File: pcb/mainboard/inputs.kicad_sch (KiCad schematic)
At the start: 95 parts

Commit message: Continued initial work on main board
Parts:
- added C122: 4.7 uF, symbol device:C
- added C123: 0.47 uF, symbol device:C
- added U30: SIT9121AI-2BF-XXS200.000000G, symbol osc-azonenberg:OSC_LVDS_NOPAD
- R101, R102: renamed from R?; footprint azonenberg_pcb:EIA_0402_RES_NOSILK -> (none)
- U8: renamed from U?; footprint azonenberg_pcb:BGA_484_22x22_FULLARRAY_1MM -> (none)
- gave numbers to parts that had none: 92
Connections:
- net 3V3: now also C122.1, C123.1, U30.1 (EN), U30.6 (VDD); no longer C73.1, C74.1, U21.7 (VDD), U22.7 (VDD)
- net DAC0_VREF: now also U21.1 (REF)
- net GND: now also C122.2, C123.2, U30.3 (GND)
- net VREF_SERDESIN: now reaches U22.11 (OUT7)
- net CLK_200_P: now reaches U8.R3 (IO_L12P_T1_MRCC_34)
- net CLK_200_P: now also U30.4 (OUT_P)
- net CLK_200_N: now reaches U8.T3 (IO_L12N_T1_MRCC_34)
- net CLK_200_N: now also U30.5 (OUT_N)
- new net 5V0: C73.1, C74.1, U21.7 (VDD), U22.7 (VDD)
- no-connect marks 4 -> 25
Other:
- note removed: "TODO: LVDS clock oscillator as main FPGA clock source"

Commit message: Calculated power monitor voltage divider
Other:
- company: (none) -> Antikernel Labs
- title: (none) -> Trigger Crossbar
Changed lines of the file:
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@@
 (kicad_sch (version 20211123) (generator eeschema)
   (paper "A2")
+  (title_block
+    (title "Trigger Crossbar")
+    (date "2023-12-17")
+    (rev "0.1")
+    (company "Antikernel Labs")
+    (comment 1 "Andrew D. Zonenberg")
+  )
   (junction (at 31.75 264.16) (diameter 0) (color 0 0 0 0)
   )

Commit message: Began assigning footprints
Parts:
- C122: footprint (none) -> azonenberg_pcb:EIA_0603_CAP_NOSILK
- C123, C59, C60, C61, C62, C63, C64, C65, C66, C67, C68, C69, C70, C71, C72, C73, C74, C75, C76: footprint (none) -> azonenberg_pcb:EIA_0402_CAP_NOSILK
- D10, D11, D12, D13, D14, D3, D4, D5, D6, D7, D8, D9: footprint (none) -> azonenberg_pcb:SOD882
- R100, R101, R102, R53, R54, R55, R56, R57, R58, R59, R60, R61, R62, R63, R64, R65, R66, R67, R68, R69, R70, R71, R72, R73, R74, R75, R76, R77, R78, R79, R80, R81, R82, R83, R84, R85, R86, R87, R88, R89, R90, R91, R92, R93, R94, R95, R96, R97, R98, R99: footprint (none) -> azonenberg_pcb:EIA_0402_RES_NOSILK
- U10, U11, U12, U13, U14, U15, U16, U17, U18, U19, U20, U9: footprint (none) -> azonenberg_pcb:DFN_8_0.5MM_2x2MM
- U21, U22: value DACx0508_WQFN -> DAC60508; footprint (none) -> azonenberg_pcb:QFN_16_0.5MM_3x3MM
- U30: footprint (none) -> azonenberg_pcb:OSCILLATOR_LVDS_3.2x2.5
- U8: footprint (none) -> azonenberg_pcb:BGA_484_22x22_FULLARRAY_1MM

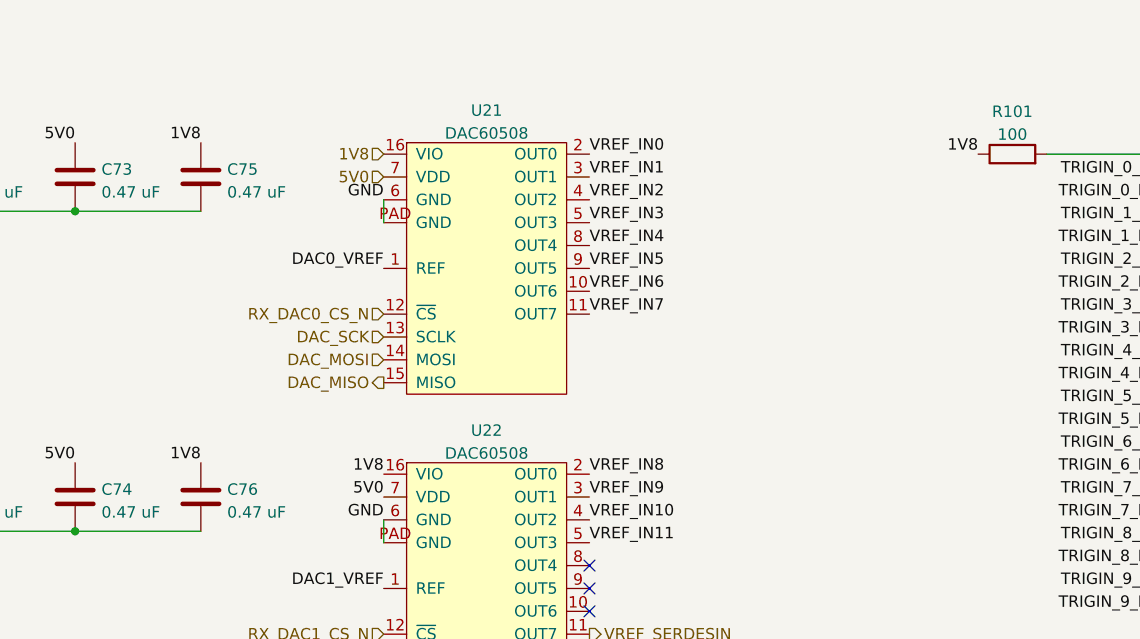
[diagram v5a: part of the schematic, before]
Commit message: Finished initial schematic review of trigger crossbar mainboard
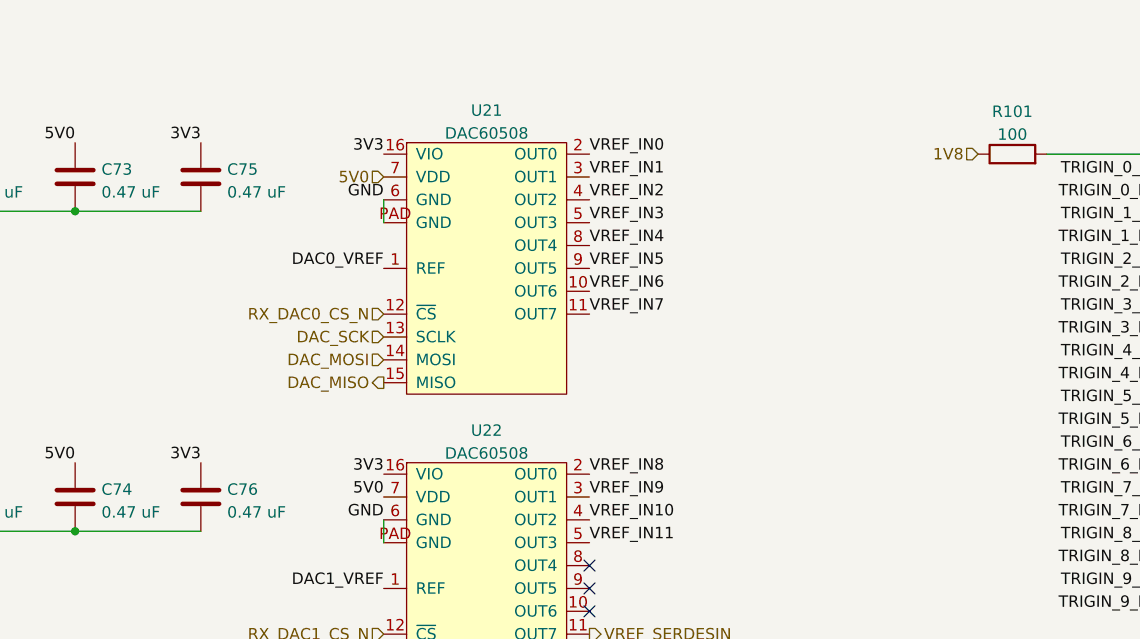
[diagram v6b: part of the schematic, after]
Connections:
- net 1V8: no longer C75.1, C76.1, U21.16 (VIO), U22.16 (VIO)
- net 3V3: now also C75.1, C76.1, U21.16 (VIO), U22.16 (VIO)
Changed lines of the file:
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@@
   (title_block
     (title "Trigger Crossbar")
-    (date "2023-12-18")
+    (date "2023-12-19")
     (rev "0.1")
     (company "Antikernel Labs")
@@
     (effects (font (size 1.27 1.27)) (justify right bottom))
   )
-  (label "1V8" (at 252.73 27.94 180)
-    (effects (font (size 1.27 1.27)) (justify right bottom))
-  )
   (label "VREF_IN8" (at 209.55 63.5 0)
     (effects (font (size 1.27 1.27)) (justify left bottom))
@@
     (effects (font (size 1.27 1.27)) (justify left bottom))
   )
-  (label "1V8" (at 166.37 62.23 180)
+  (label "3V3" (at 166.37 62.23 180)
     (effects (font (size 1.27 1.27)) (justify right bottom))
   )
@@
     (effects (font (size 1.27 1.27)) (justify right bottom))
   )
-  (label "1V8" (at 186.69 63.5 180)
+  (label "3V3" (at 186.69 63.5 180)
     (effects (font (size 1.27 1.27)) (justify right bottom))
   )
@@
     (effects (font (size 1.27 1.27)) (justify right bottom))
   )
-  (label "1V8" (at 166.37 26.67 180)
+  (label "3V3" (at 166.37 26.67 180)
     (effects (font (size 1.27 1.27)) (justify right bottom))
   )
@@
     (effects (font (size 1.27 1.27)) (justify right bottom))
   )
+  (label "3V3" (at 186.69 27.94 180)
+    (effects (font (size 1.27 1.27)) (justify right bottom))
+  )
   (label "GND" (at 69.85 312.42 180)
     (effects (font (size 1.27 1.27)) (justify right bottom))
@@
   )
   (hierarchical_label "IN0" (shape input) (at 26.67 34.29 180)
-    (effects (font (size 1.27 1.27)) (justify right))
-  )
-  (hierarchical_label "1V8" (shape input) (at 186.69 27.94 180)
     (effects (font (size 1.27 1.27)) (justify right))
   )
@@
     (effects (font (size 1.27 1.27)) (justify right))
   )
+  (hierarchical_label "1V8" (shape input) (at 252.73 27.94 180)
+    (effects (font (size 1.27 1.27)) (justify right))
+  )

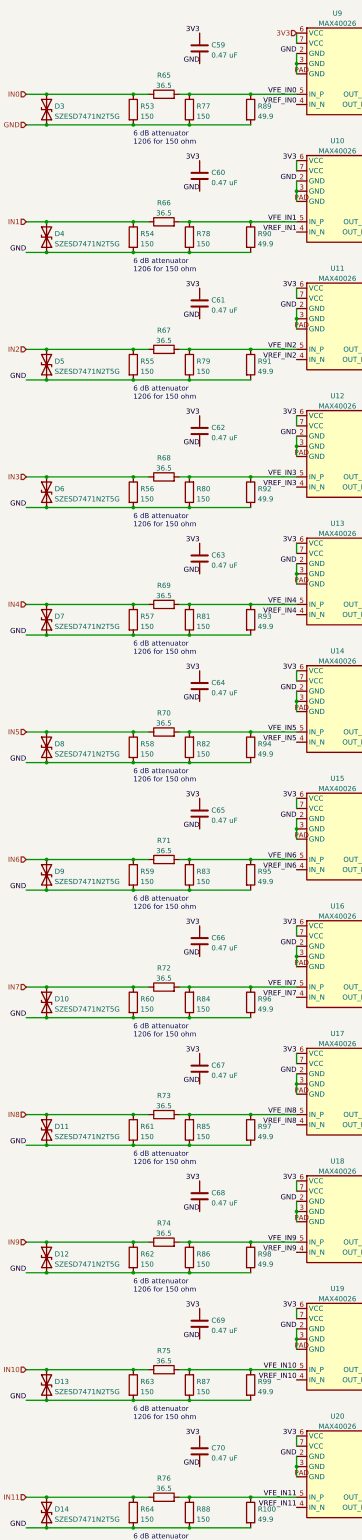
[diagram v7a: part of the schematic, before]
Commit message: Started layout of rear panel IO connectors and associated drivers/comparators
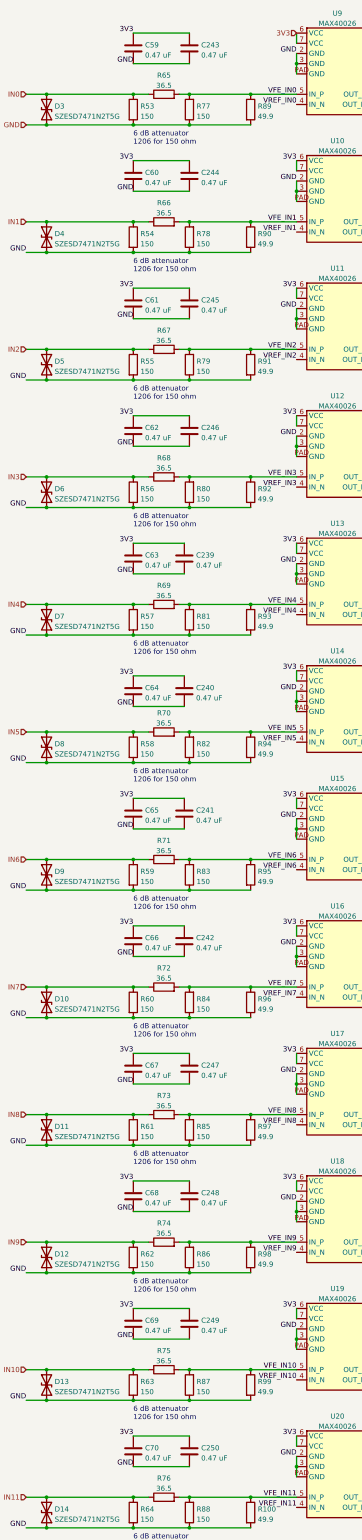
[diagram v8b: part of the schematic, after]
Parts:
- added C239, C240, C241, C242, C243, C244, C245, C246, C247, C248, C249, C250: 0.47 uF, azonenberg_pcb:EIA_0402_CAP_NOSILK, symbol device:C
- R53, R54, R55, R56, R57, R58, R59, R60, R61, R62, R63, R64, R77, R78, R79, R80, R81, R82, R83, R84, R85, R86, R87, R88: footprint azonenberg_pcb:EIA_0402_RES_NOSILK -> azonenberg_pcb:EIA_1206_CAP_NOSILK
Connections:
- net 3V3: now also C239.1, C240.1, C241.1, C242.1, C243.1, C244.1, C245.1, C246.1, C247.1, C248.1, C249.1, C250.1
- net GND: now also C239.2, C240.2, C241.2, C242.2, C243.2, C244.2, C245.2, C246.2, C247.2, C248.2, C249.2, C250.2
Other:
- moved on the sheet: C59, C60, C61, C62, C63, C64, C65, C66, C67, C68, C69, C70
